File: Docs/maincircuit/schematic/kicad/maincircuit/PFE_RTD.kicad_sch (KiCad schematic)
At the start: 11 parts, among them U5 MCP6042, U6 MCP6042, U7 MCP6042

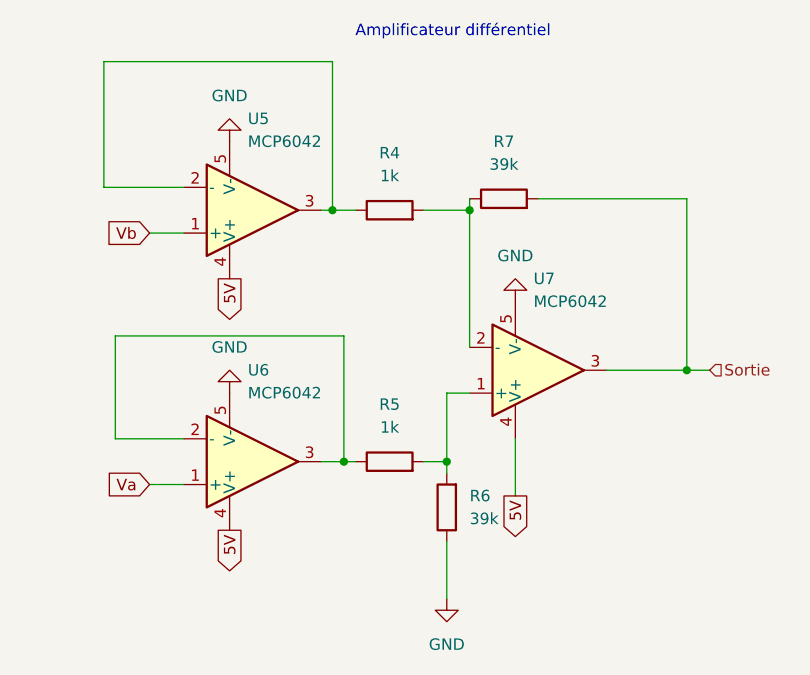
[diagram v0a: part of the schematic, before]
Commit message: correction pour les pin des MCP6042; generer le bom
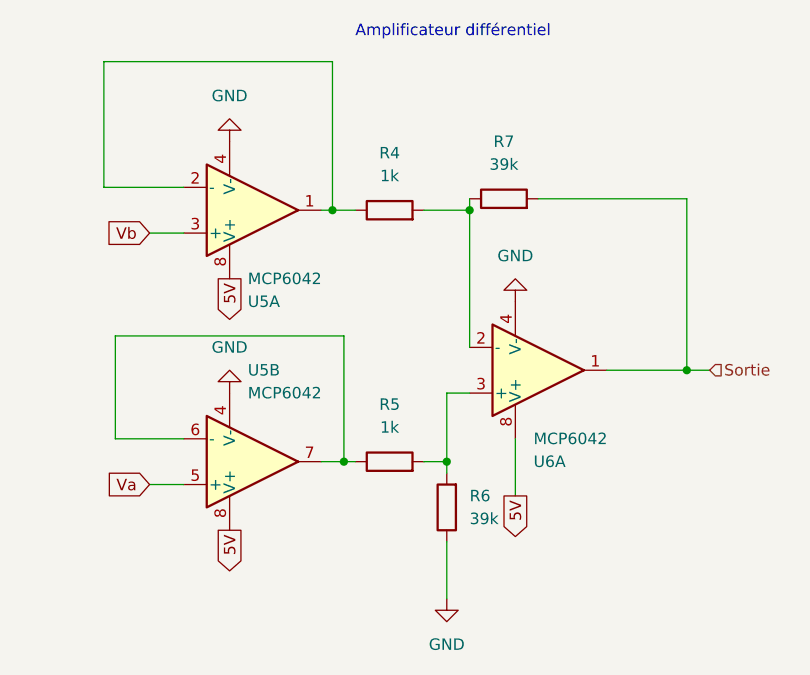
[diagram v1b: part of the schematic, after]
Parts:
- removed U7: MCP6042, symbol pspice:OPAMP
- added unit 2 of U5
- U5, U6: Spice_Node_Sequence 1 2 4 5 3 -> 1 2 4 5 3
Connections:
- net 5V: now also U5.8 (V+), U6.8 (V+), U5.8 (V+); no longer U5.4 (V+), U6.4 (V+)
- net GND: now also U5.4 (V-), U6.4 (V-), U5.4 (V-); no longer U5.5 (V-), U6.5 (V-)
- net Sortie: now also U6.1
- net Va: now also U5.5 (+); no longer U6.1 (+)
- net Vb: now also U5.3 (+); no longer U5.1 (+)
- net at R4.2, R7.1: now also U6.2 (-)
- net at R5.2, R6.2: now also U6.3 (+)
- net at R4.1, U5.2 (-): now also U5.1; no longer U5.3
- new net: R5.1, U5.6 (-), U5.7
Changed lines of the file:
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@@
   (title_block
     (title "RTD PT100 - Circuit d'adaptation")
-    (date "2022-04-05")
-    (rev "1.0")
+    (date "2022-04-07")
+    (rev "1.1")
     (company "ÉTS - PFE HIVER 2022 - ELE795")
     (comment 1 "NASRI, Mahan")
@@
     (effects (font (size 1.27 1.27)) (justify left))
   )
+  (symbol (lib_name "OPAMP_2") (lib_id "pspice:OPAMP") (at 157.48 119.38 0) (mirror x) (unit 2)
+    (in_bom yes) (on_board yes) (fields_autoplaced)
+    (property "Reference" "U5" (id 0) (at 156.9594 109.22 0)
+      (effects (font (size 1.27 1.27)) (justify left))
+    )
+    (property "Value" "MCP6042" (id 1) (at 156.9594 111.76 0)
+      (effects (font (size 1.27 1.27)) (justify left))
+    )
+    (property "Footprint" "" (id 2) (at 157.48 119.38 0)
+      (effects (font (size 1.27 1.27)) hide)
+    )
+    (property "Datasheet" "~" (id 3) (at 157.48 119.38 0)
+      (effects (font (size 1.27 1.27)) hide)
+    )
+    (property "Spice_Primitive" "X" (id 4) (at 157.48 119.38 0)
+      (effects (font (size 1.27 1.27)) hide)
+    )
+    (property "Spice_Model" "MCP6041" (id 5) (at 157.48 119.38 0)
+      (effects (font (size 1.27 1.27)) hide)
+    )
+    (property "Spice_Netlist_Enabled" "Y" (id 6) (at 157.48 119.38 0)
+      (effects (font (size 1.27 1.27)) hide)
+    )
+    (property "Spice_Lib_File" "MCP604x/MCP6041.txt" (id 7) (at 157.48 119.38 0)
+      (effects (font (size 1.27 1.27)) hide)
+    )
+    (property "Spice_Node_Sequence" "1 2 4 5 3" (id 8) (at 157.48 119.38 0)
+      (effects (font (size 1.27 1.27)) hide)
+    )
+    (pin "7")
+    (pin "6")
+    (pin "5")
+    (pin "4")
+    (pin "8")
+  )
   (symbol (lib_id "power:GND") (at 99.06 123.19 0) (unit 1)
     (in_bom yes) (on_board yes) (fields_autoplaced)
@@
     (pin "2")
   )
-  (symbol (lib_id "pspice:OPAMP") (at 157.48 119.38 0) (mirror x) (unit 1)
-    (in_bom yes) (on_board yes) (fields_autoplaced)
-    (property "Reference" "U6" (id 0) (at 156.9594 109.22 0)
-      (effects (font (size 1.27 1.27)) (justify left))
-    )
-    (property "Value" "MCP6042" (id 1) (at 156.9594 111.76 0)
-      (effects (font (size 1.27 1.27)) (justify left))
-    )
-    (property "Footprint" "" (id 2) (at 157.48 119.38 0)
-      (effects (font (size 1.27 1.27)) hide)
-    )
-    (property "Datasheet" "~" (id 3) (at 157.48 119.38 0)
-      (effects (font (size 1.27 1.27)) hide)
-    )
-    (property "Spice_Primitive" "X" (id 4) (at 157.48 119.38 0)
-      (effects (font (size 1.27 1.27)) hide)
-    )
-    (property "Spice_Model" "MCP6041" (id 5) (at 157.48 119.38 0)
-      (effects (font (size 1.27 1.27)) hide)
-    )
-    (property "Spice_Netlist_Enabled" "Y" (id 6) (at 157.48 119.38 0)
-      (effects (font (size 1.27 1.27)) hide)
-    )
-    (property "Spice_Lib_File" "MCP604x/MCP6041.txt" (id 7) (at 157.48 119.38 0)
-      (effects (font (size 1.27 1.27)) hide)
-    )
-    (property "Spice_Node_Sequence" "1  2 4 5 3" (id 8) (at 157.48 119.38 0)
-      (effects (font (size 1.27 1.27)) hide)
-    )
-    (pin "1")
-    (pin "2")
-    (pin "3")
-    (pin "4")
-    (pin "5")
-  )
   (symbol (lib_id "Device:R") (at 172.72 119.38 90) (unit 1)
     (in_bom yes) (on_board yes) (fields_autoplaced)
@@
     (pin "2")
   )
+  (symbol (lib_name "OPAMP_1") (lib_id "pspice:OPAMP") (at 189.23 109.22 0) (mirror x) (unit 1)
+    (in_bom yes) (on_board yes) (fields_autoplaced)
+    (property "Reference" "U6" (id 0) (at 188.7094 119.38 0)
+      (effects (font (size 1.27 1.27)) (justify left))
+    )
+    (property "Value" "MCP6042" (id 1) (at 188.7094 116.84 0)
+      (effects (font (size 1.27 1.27)) (justify left))
+    )
+    (property "Footprint" "" (id 2) (at 189.23 109.22 0)
+      (effects (font (size 1.27 1.27)) hide)
+    )
+    (property "Datasheet" "~" (id 3) (at 189.23 109.22 0)
+      (effects (font (size 1.27 1.27)) hide)
+    )
+    (property "Spice_Primitive" "X" (id 4) (at 189.23 109.22 0)
+      (effects (font (size 1.27 1.27)) hide)
+    )
+    (property "Spice_Model" "MCP6041" (id 5) (at 189.23 109.22 0)
+      (effects (font (size 1.27 1.27)) hide)
+    )
+    (property "Spice_Netlist_Enabled" "Y" (id 6) (at 189.23 109.22 0)
+      (effects (font (size 1.27 1.27)) hide)
+    )
+    (property "Spice_Lib_File" "MCP604x/MCP6041.txt" (id 7) (at 189.23 109.22 0)
+      (effects (font (size 1.27 1.27)) hide)
+    )
+    (property "Spice_Node_Sequence" "1 2 4 5 3" (id 8) (at 189.23 109.22 0)
+      (effects (font (size 1.27 1.27)) hide)
+    )
+    (pin "1")
+    (pin "2")
+    (pin "3")
+    (pin "4")
+    (pin "8")
+  )
   (symbol (lib_id "power:GND") (at 186.69 101.6 180) (unit 1)
     (in_bom yes) (on_board yes) (fields_autoplaced)
@@
     (pin "1")
   )
-  (symbol (lib_id "pspice:OPAMP") (at 157.48 91.44 0) (mirror x) (unit 1)
-    (in_bom yes) (on_board yes) (fields_autoplaced)
-    (property "Reference" "U5" (id 0) (at 156.9594 81.28 0)
-      (effects (font (size 1.27 1.27)) (justify left))
-    )
-    (property "Value" "MCP6042" (id 1) (at 156.9594 83.82 0)
+  (symbol (lib_name "OPAMP_1") (lib_id "pspice:OPAMP") (at 157.48 91.44 0) (mirror x) (unit 1)
+    (in_bom yes) (on_board yes) (fields_autoplaced)
+    (property "Reference" "U5" (id 0) (at 156.9594 101.6 0)
+      (effects (font (size 1.27 1.27)) (justify left))
+    )
+    (property "Value" "MCP6042" (id 1) (at 156.9594 99.06 0)
       (effects (font (size 1.27 1.27)) (justify left))
     )
@@
       (effects (font (size 1.27 1.27)) hide)
     )
-    (property "Spice_Node_Sequence" "1  2 4 5 3" (id 8) (at 157.48 91.44 0)
+    (property "Spice_Node_Sequence" "1 2 4 5 3" (id 8) (at 157.48 91.44 0)
       (effects (font (size 1.27 1.27)) hide)
     )
@@
     (pin "3")
     (pin "4")
-    (pin "5")
+    (pin "8")
   )
   (symbol (lib_id "power:GND") (at 154.94 83.82 180) (unit 1)
@@
     (pin "2")
   )
-  (symbol (lib_id "pspice:OPAMP") (at 189.23 109.22 0) (mirror x) (unit 1)
-    (in_bom yes) (on_board yes) (fields_autoplaced)
-    (property "Reference" "U7" (id 0) (at 188.7094 99.06 0)
-      (effects (font (size 1.27 1.27)) (justify left))
-    )
-    (property "Value" "MCP6042" (id 1) (at 188.7094 101.6 0)
-      (effects (font (size 1.27 1.27)) (justify left))
-    )
-    (property "Footprint" "" (id 2) (at 189.23 109.22 0)
-      (effects (font (size 1.27 1.27)) hide)
-    )
-    (property "Datasheet" "~" (id 3) (at 189.23 109.22 0)
-      (effects (font (size 1.27 1.27)) hide)
-    )
-    (property "Spice_Primitive" "X" (id 4) (at 189.23 109.22 0)
-      (effects (font (size 1.27 1.27)) hide)
-    )
-    (property "Spice_Model" "MCP6041" (id 5) (at 189.23 109.22 0)
-      (effects (font (size 1.27 1.27)) hide)
-    )
-    (property "Spice_Netlist_Enabled" "Y" (id 6) (at 189.23 109.22 0)
-      (effects (font (size 1.27 1.27)) hide)
-    )
-    (property "Spice_Lib_File" "MCP604x/MCP6041.txt" (id 7) (at 189.23 109.22 0)
-      (effects (font (size 1.27 1.27)) hide)
-    )
-    (property "Spice_Node_Sequence" "1  2 4 5 3" (id 8) (at 189.23 109.22 0)
-      (effects (font (size 1.27 1.27)) hide)
-    )
-    (pin "1")
-    (pin "2")
-    (pin "3")
-    (pin "4")
-    (pin "5")
-  )
   (symbol (lib_id "power:GND") (at 179.07 134.62 0) (unit 1)

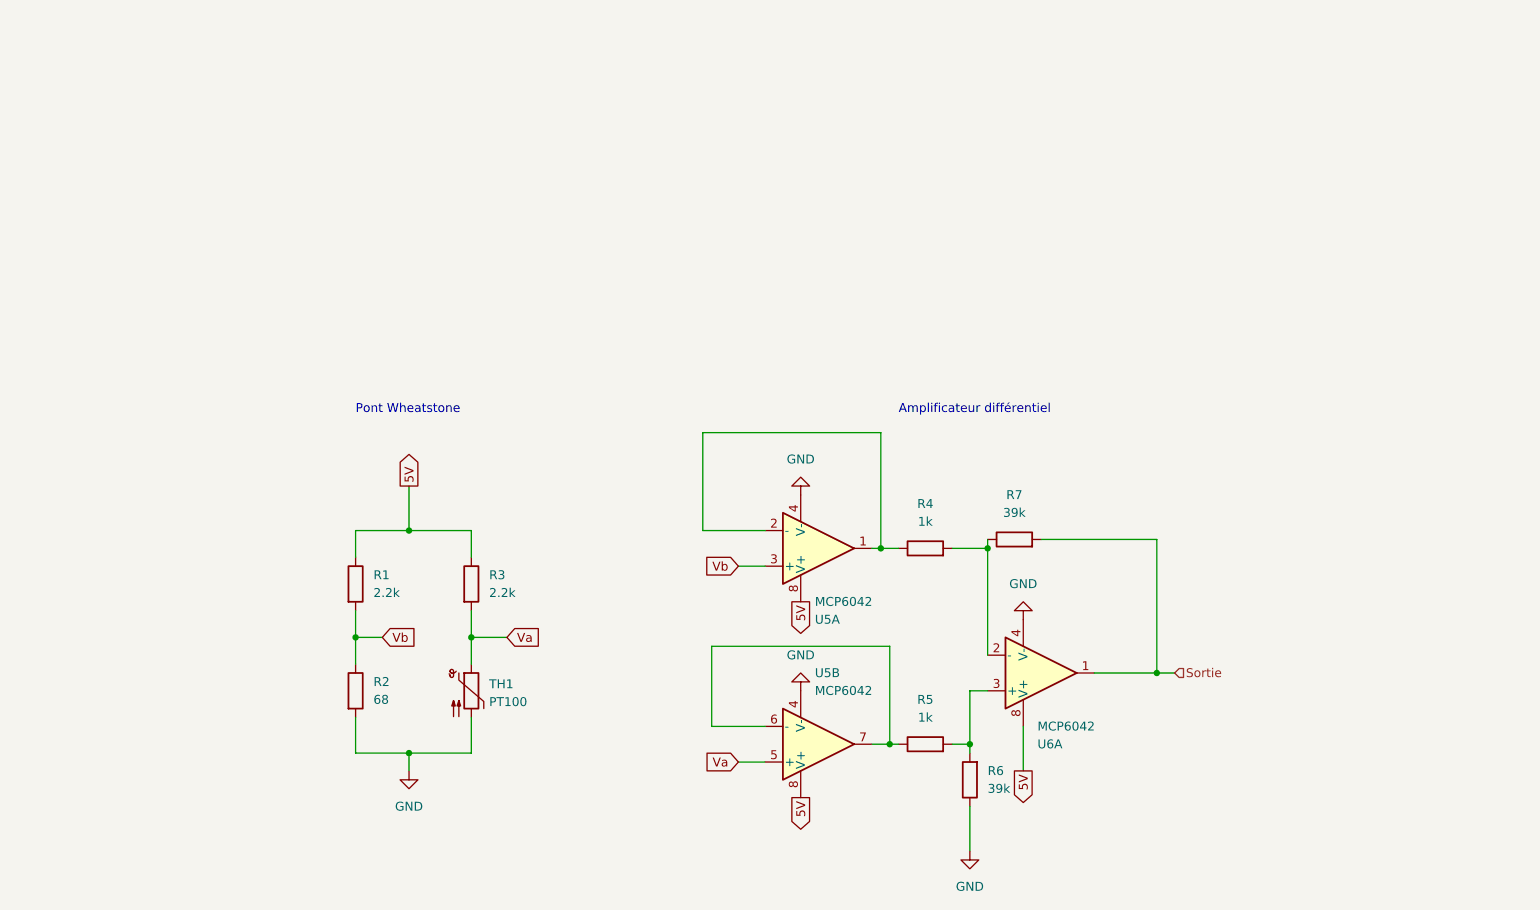
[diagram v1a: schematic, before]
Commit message: diagramme de circuit version 1.2 : ajout du circuit de relais + modif
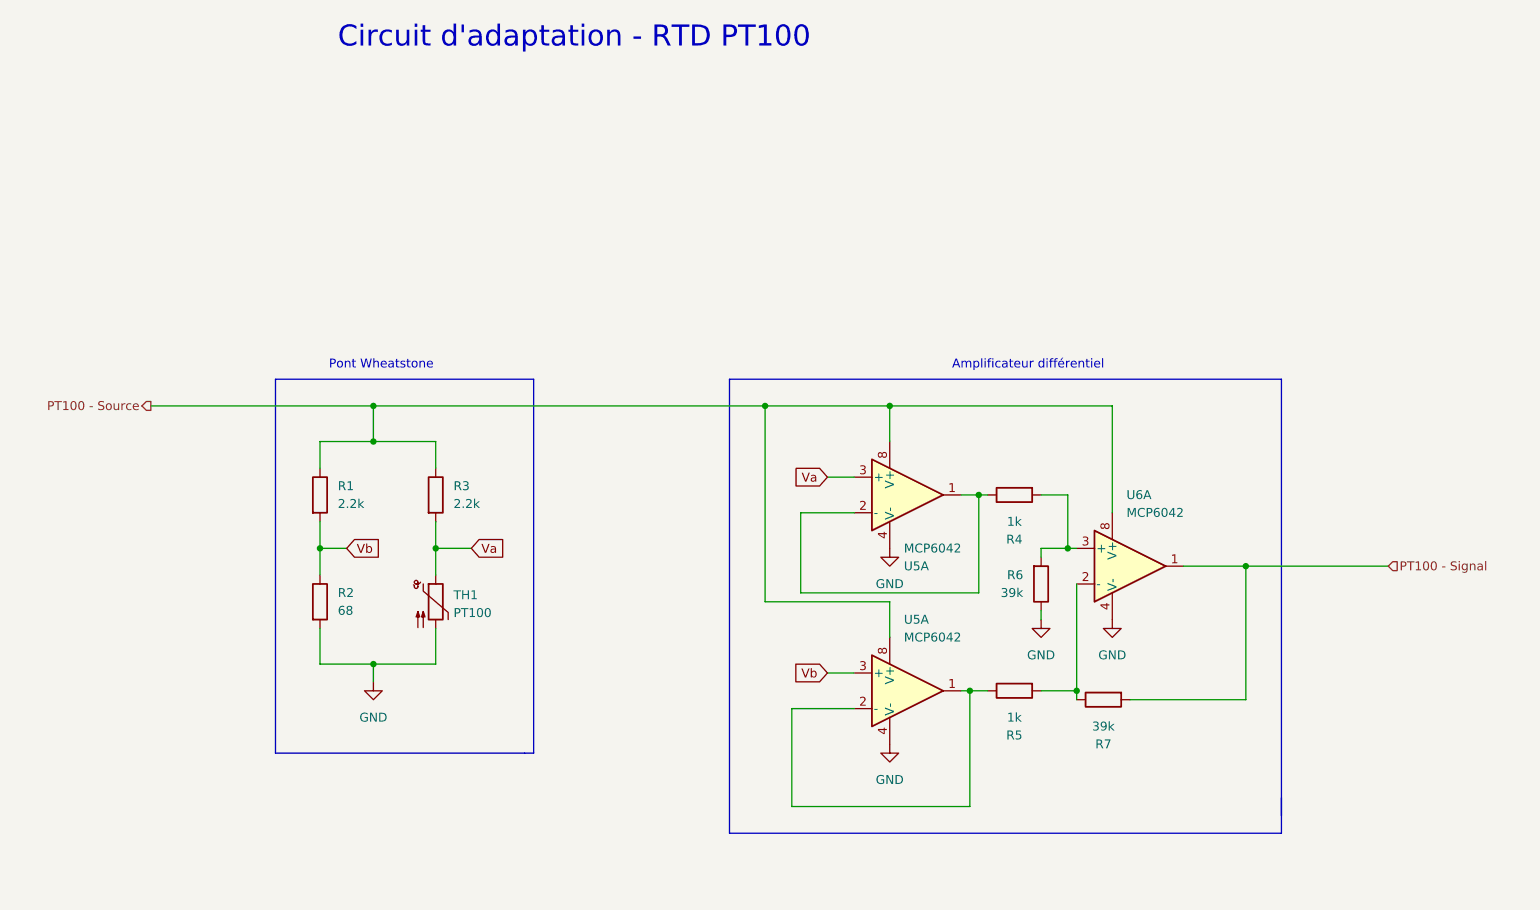
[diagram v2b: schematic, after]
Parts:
- renumbered R5 to R4, R4 to R5
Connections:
- net Va: now also U5.3 (+); no longer U5.5 (+)
- net 5V renamed PT100 - Source
- net Sortie renamed PT100 - Signal
- new net: R4.1, U5.1, U5.2 (-)
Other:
- note added: "Circuit d'adaptation - RTD PT100"
- title: RTD PT100 - Circuit d'adaptation -> Circuit d'adaptation PT100
- moved on the sheet: R1, R2, R3, R4, R5, R6, R7, TH1, U5A, U6A
